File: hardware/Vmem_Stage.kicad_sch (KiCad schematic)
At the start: 12 parts, among them U3001 AOZ5276QI, U3002 AOZ5276QI

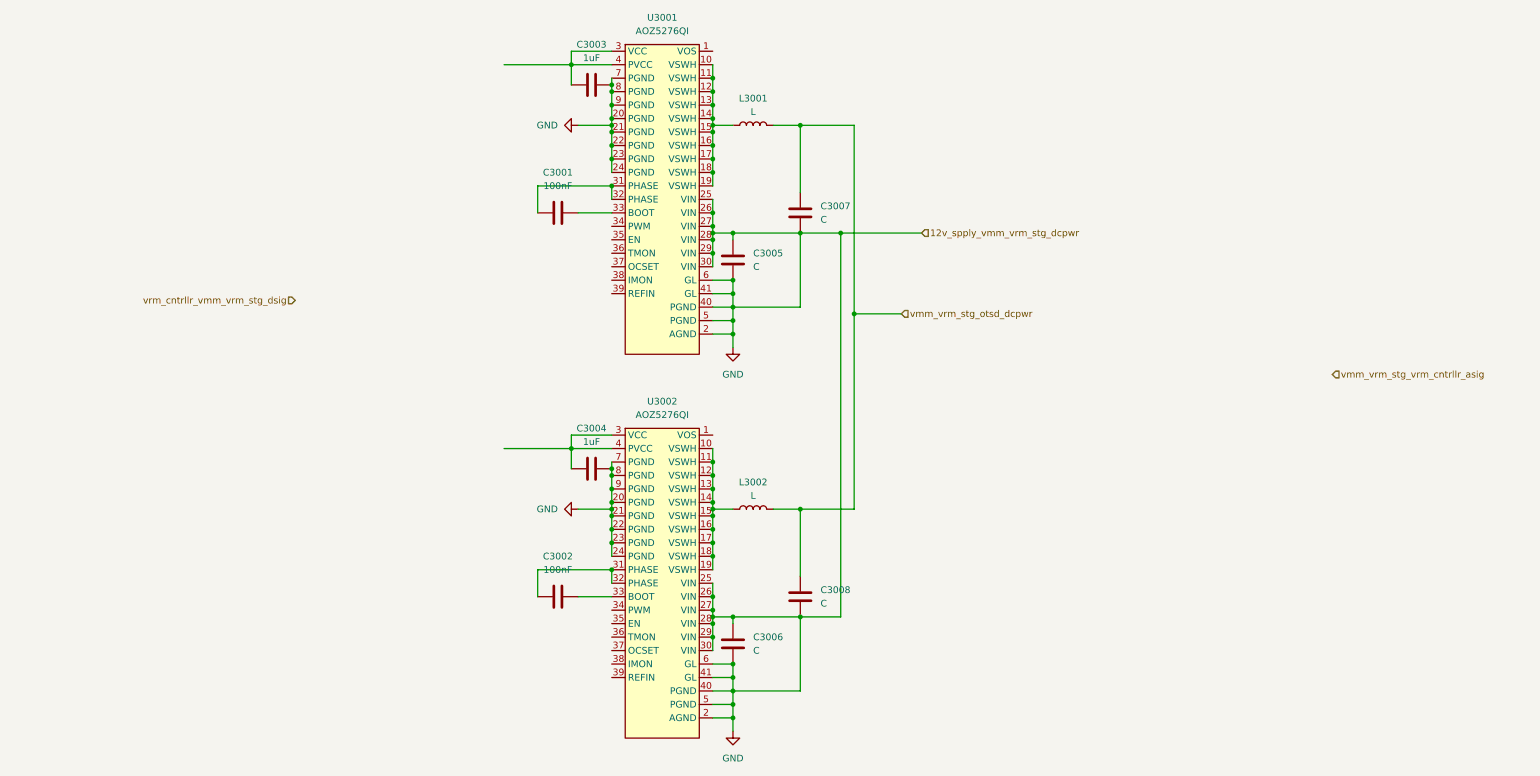
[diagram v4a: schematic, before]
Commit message: rebase(schematic): Updated Vcore and Vmem pins
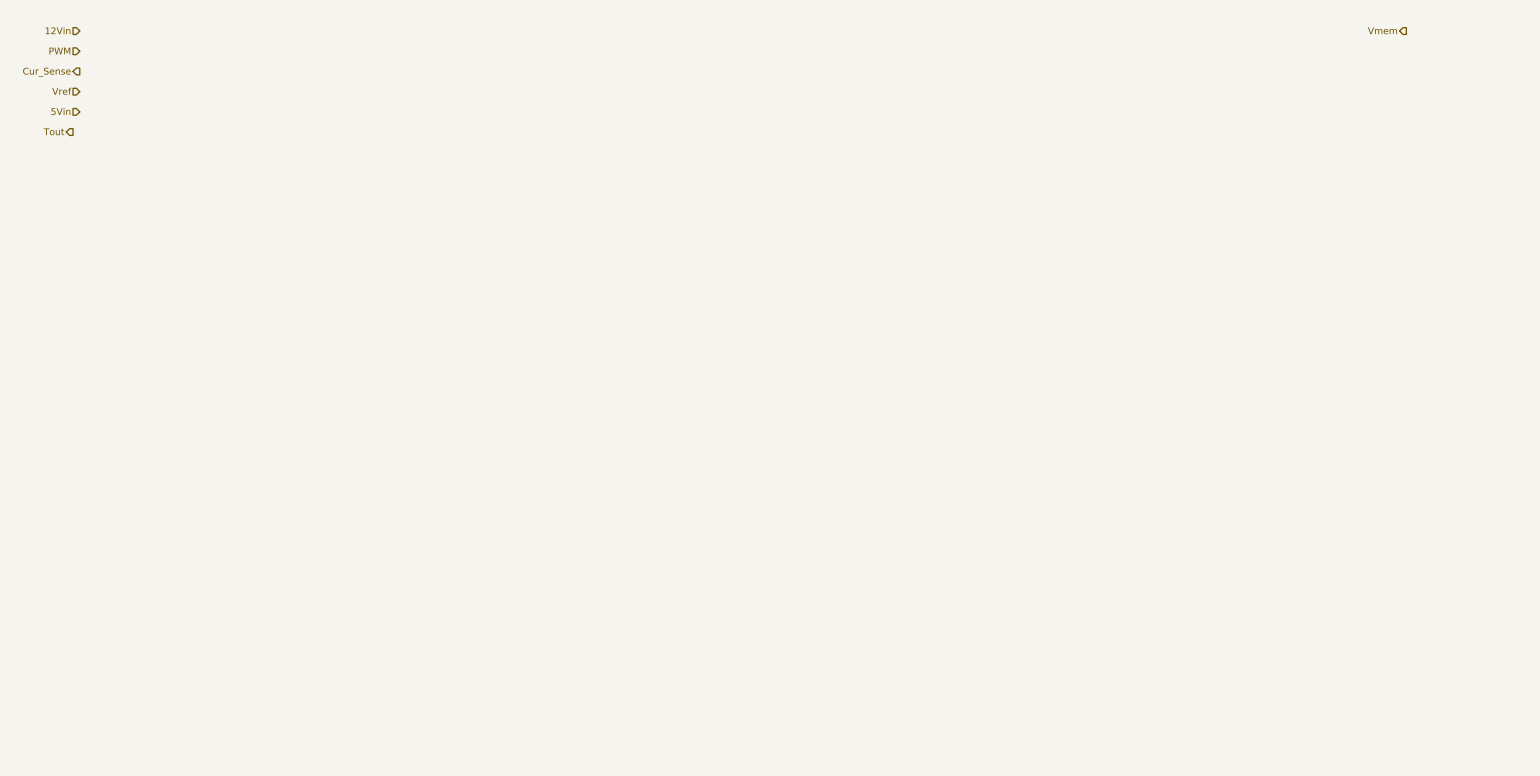
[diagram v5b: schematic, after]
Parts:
- removed C3001, C3002: 100nF, symbol Device:C
- removed C3003, C3004: 1uF, symbol Device:C
- removed C3005, C3006, C3007, C3008: C, symbol Device:C
- removed L3001, L3002: L, symbol Device:L
- removed U3001, U3002: AOZ5276QI, symbol Symbol_Library:AOZ5276QI
